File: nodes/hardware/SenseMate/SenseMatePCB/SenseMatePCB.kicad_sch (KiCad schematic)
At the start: 16 parts, among them M1 Motor_DC, Q1 2SC1815, Q2 2SC1815, SW1 SW_Push, SW2 SW_Push, SW3 SW_Push, SW5 SW_DPDT_x2

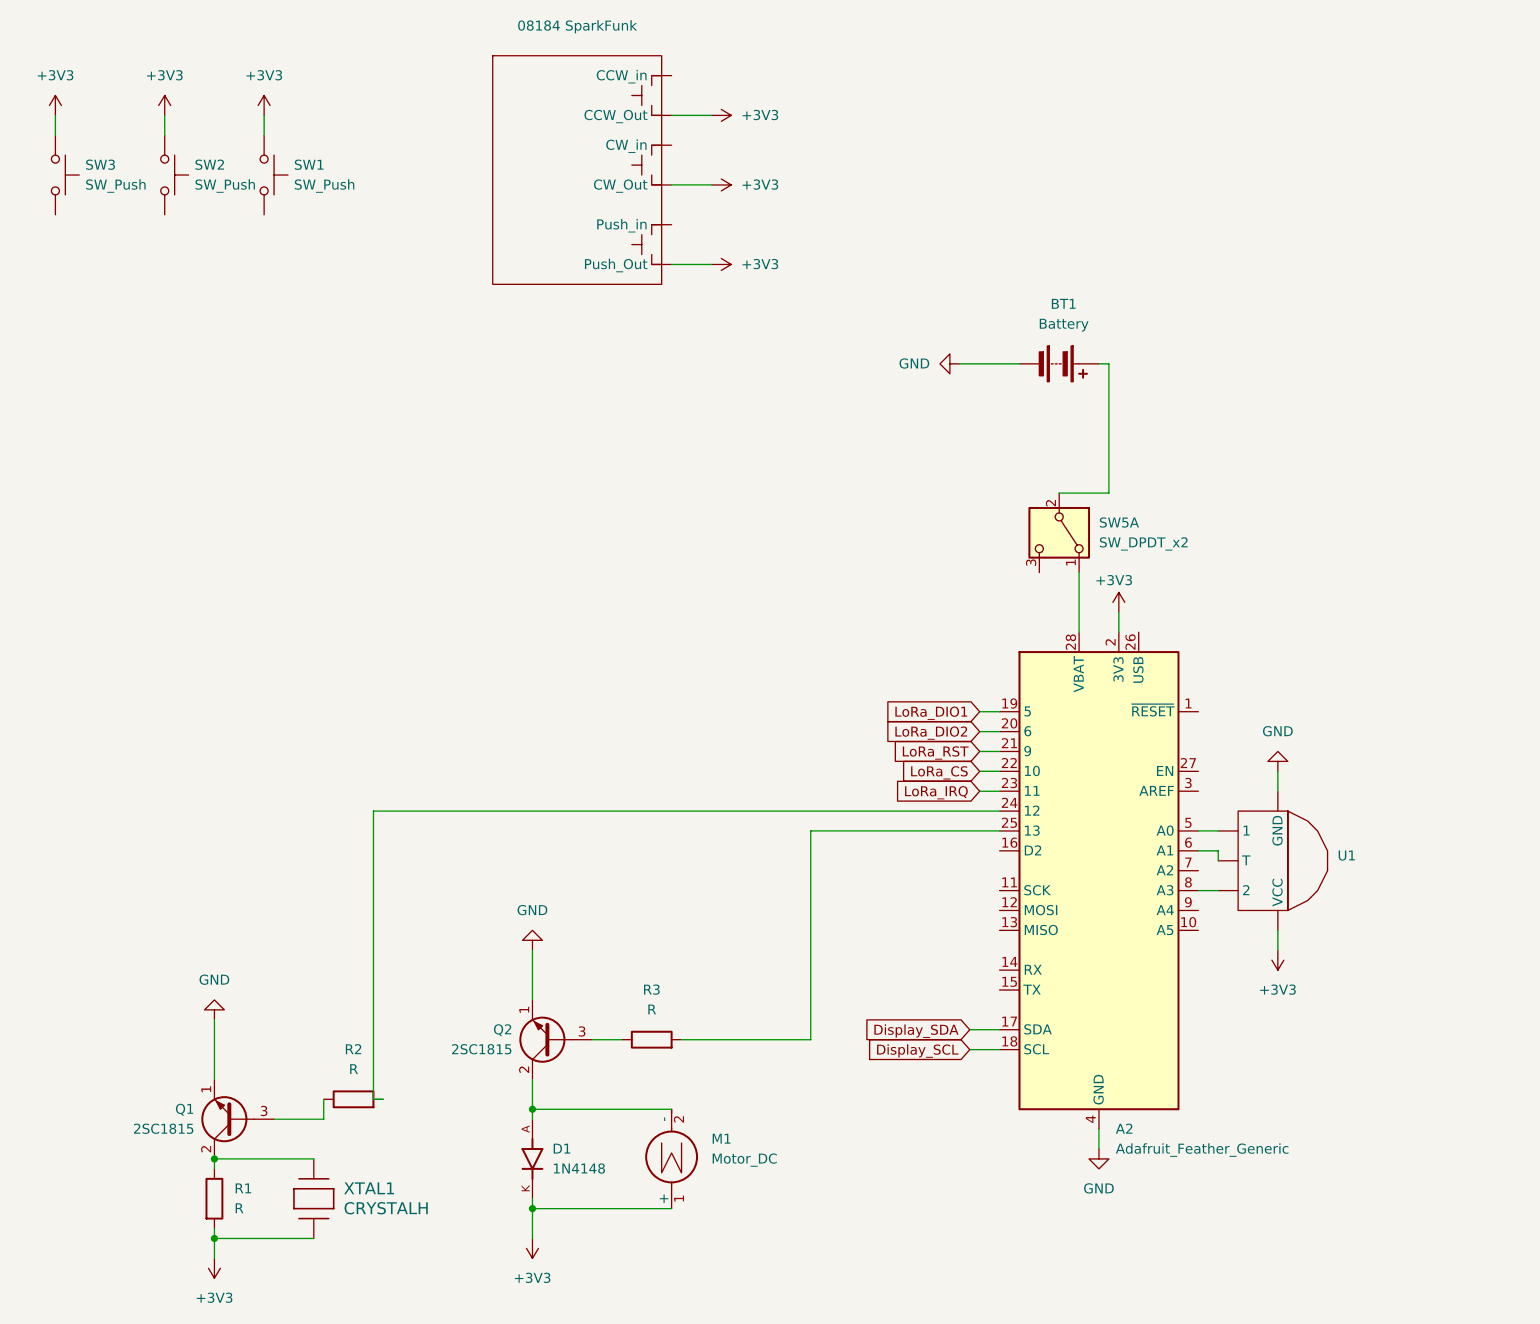
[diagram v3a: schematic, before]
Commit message: finished schmatic and footprint assignement issue#02 and issue#03
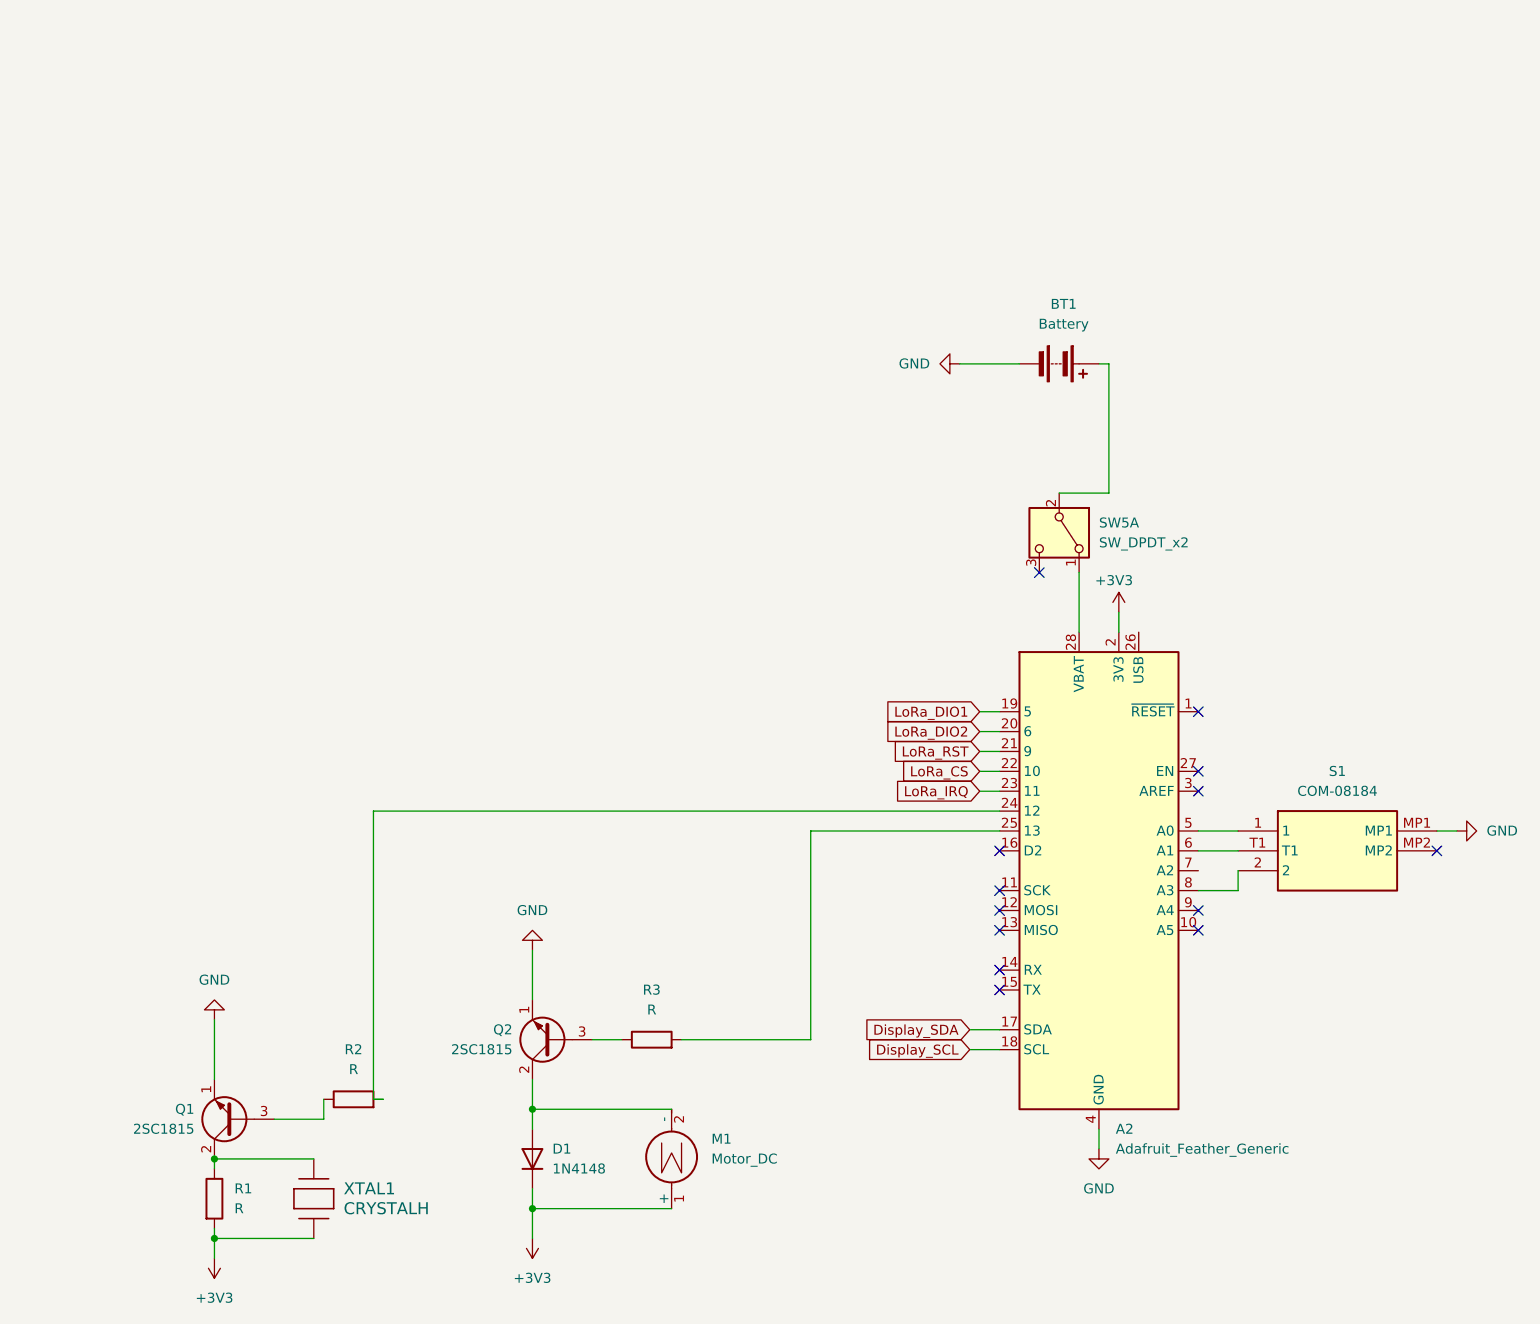
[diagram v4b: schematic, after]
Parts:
- removed 08184 SparkFunk: ~, symbol FeatherSense_PushButton:_1
- removed D1: 1N4148, 1N4148:DIOAD753W49L380D172B, symbol FeatherSense_1N4148:1N4148
- removed SW1, SW2, SW3: SW_Push, symbol Switch:SW_Push
- removed U1: ~, symbol FeatherSense_JoyButton:08184_SparkFunk
- added D1: 1N4148, Diode_THT:D_DO-35_SOD27_P7.62mm_Horizontal, symbol Diode:1N4148
- added S1: COM-08184, SenseMate_sw_fp:COM08184, symbol SenseMate_COM-08184:COM-08184
- BT1, M1: footprint (none) -> Connector_JST:JST_PH_S2B-PH-K_1x02_P2.00mm_Horizontal
- R1, R2, R3: footprint (none) -> Resistor_SMD:R_0805_2012Metric
- SW5: footprint (none) -> SenseMate_Pwr_Button_:OS102011MA1QN1
- XTAL1: footprint XTAL_PS1240P02BT_TDK -> SenseMate_sound:PS1240P02BT
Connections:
- net +3V3: now also D1.1 (K)
- net GND: now also S1.MP1
- net at A2.5 (A0): now also S1.1
- net at A2.6 (A1): now also S1.T1
- net at A2.8 (A3): now also S1.2
- net at M1.2 (-), Q2.2 (C): now also D1.2 (A)
- no-connect marks 0 -> 13

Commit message: run erc and startet pcb design an routing issue#4
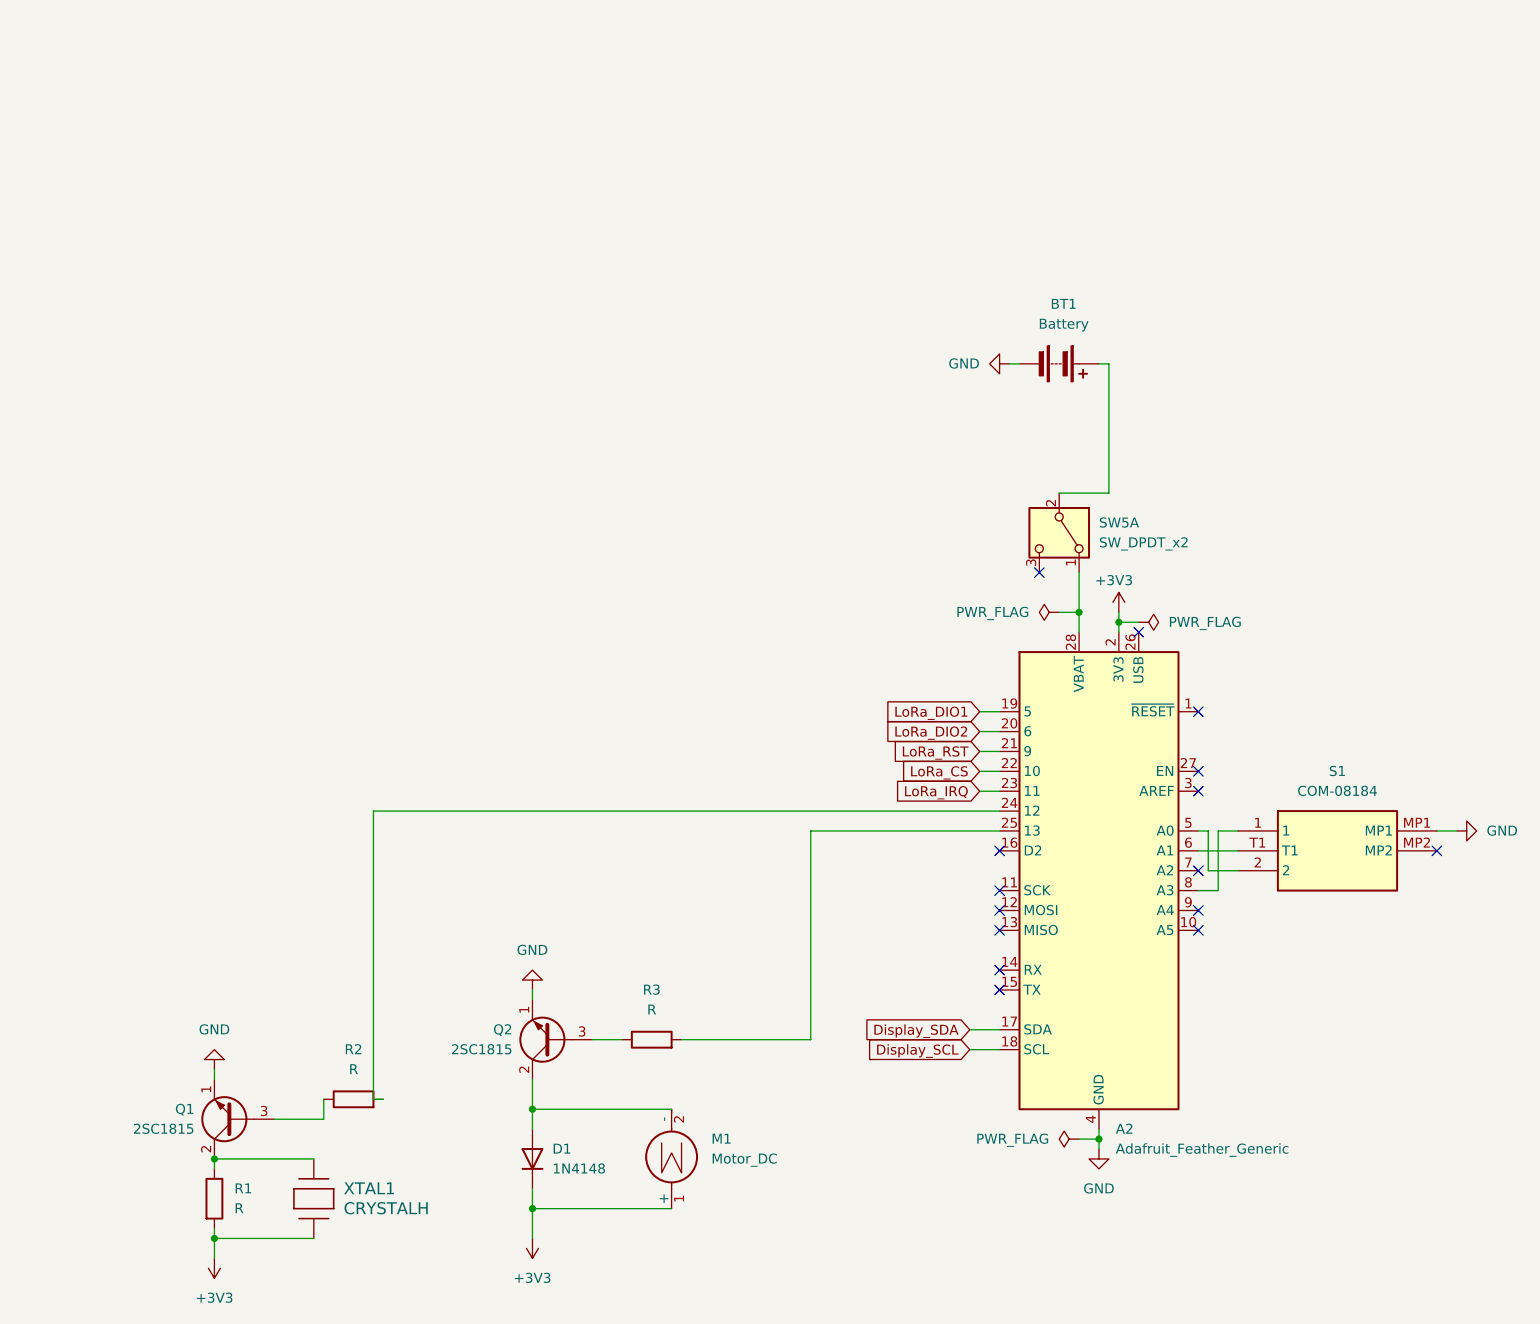
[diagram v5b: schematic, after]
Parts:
- XTAL1: footprint SenseMate_sound:PS1240P02BT -> XTAL_PS1240P02BT_TDK
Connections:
- net at A2.5 (A0): now also S1.2; no longer S1.1
- net at A2.8 (A3): now also S1.1; no longer S1.2
- no-connect marks 13 -> 15
